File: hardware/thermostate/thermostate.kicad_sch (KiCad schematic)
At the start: 17 parts

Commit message: Finnish ESP32 SCH, NOT revision
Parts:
- added C1, C2: 0.1uF/50V(20%), symbol Device:C
- added D5: SK6812MINI, LED_SMD:LED_SK6812MINI_PLCC4_3.5x3.5mm_P1.75mm, symbol LED:SK6812MINI
- added IC1, IC2: L8050QLT1G, L8050QLT1G, symbol L8050QLT1G:L8050QLT1G
- added R1, R2: 10k(1%), symbol Device:R
- added R4, R5: 0(1%), symbol Device:R
- added SW1, SW2: SW_Push, symbol Switch:SW_Push
- gave numbers to parts that had none: 17
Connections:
- net +3V3: now also D5.4 (VDD)
- net CHIP_PU: now also C2.2, R4.1, SW2.2
- net GND: now also C1.1, C2.1, D5.2 (VSS), SW1.1, SW2.1
- net GPIO0: now reaches U1.27 (GPIO0/BOOT)
- net GPIO0: now also C1.2, R5.1, SW1.2
- net GPIO38: now reaches U1.31 (GPIO38/FSPIWP/SUBSPIWP)
- net GPIO38: now also D5.1 (DOUT)
- new net: IC1.1 (B), R1.2
- new net: IC1.3 (C), R4.2
- new net: IC2.3 (C), R5.2
- new net DTR: IC2.1 (B), IC2.2 (E), R1.1, R2.2
- new net RTS: IC1.2 (E), R2.1
- no-connect marks 1 -> 2
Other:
- moved on the sheet: C3, C4

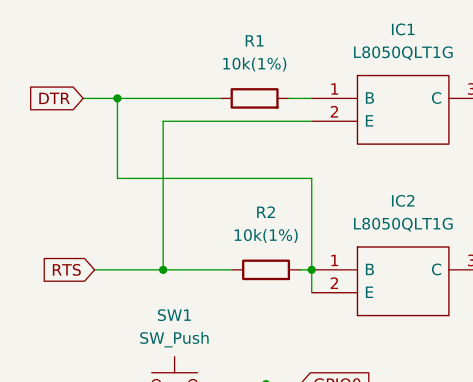
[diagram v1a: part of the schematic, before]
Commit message: Add LCSC row
Signed-off-by: Javier <javierfernandezvillasante@gmail.com>
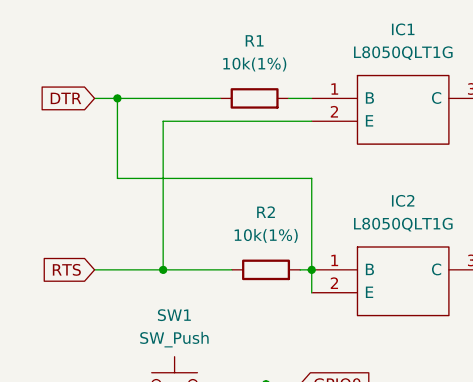
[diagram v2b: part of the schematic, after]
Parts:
- R1, R2: footprint (none) -> Resistor_SMD:R_0805_2012Metric; LCSC Part# (none) -> C269742
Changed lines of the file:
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@@
     (stroke (width 0) (type default) (color 0 0 0 0))
   )
-  (wire (pts (xy 22.86 34.29) (xy 19.05 34.29))
+  (wire (pts (xy 22.86 34.29) (xy 20.32 34.29))
     (stroke (width 0) (type default) (color 0 0 0 0))
   )
@@
     )
   )
-  (global_label "DTR" (shape input) (at 19.05 34.29 180) (fields_autoplaced)
+  (global_label "DTR" (shape input) (at 20.32 34.29 180) (fields_autoplaced)
     (effects (font (size 1.27 1.27)) (justify right))
-    (property "Intersheet References" "${INTERSHEET_REFS}" (id 0) (at 13.1293 34.2106 0)
+    (property "Intersheet References" "${INTERSHEET_REFS}" (id 0) (at 14.3993 34.2106 0)
       (effects (font (size 1.27 1.27)) (justify right) hide)
     )
@@
     (property "Reference" "R2" (id 0) (at 39.37 46.99 90))
     (property "Value" "10k(1%)" (id 1) (at 39.37 49.53 90))
-    (property "Footprint" "" (id 2) (at 39.37 55.118 90)
+    (property "Footprint" "Resistor_SMD:R_0805_2012Metric" (id 2) (at 39.37 55.118 90)
       (effects (font (size 1.27 1.27)) hide)
     )
     (property "Datasheet" "~" (id 3) (at 39.37 53.34 0)
+      (effects (font (size 1.27 1.27)) hide)
+    )
+    (property "LCSC Part#" "C269742" (id 4) (at 39.37 53.34 0)
       (effects (font (size 1.27 1.27)) hide)
     )
@@
     (property "Reference" "R1" (id 0) (at 38.1 27.94 90))
     (property "Value" "10k(1%)" (id 1) (at 38.1 30.48 90))
-    (property "Footprint" "" (id 2) (at 38.1 36.068 90)
+    (property "Footprint" "Resistor_SMD:R_0805_2012Metric" (id 2) (at 38.1 36.068 90)
       (effects (font (size 1.27 1.27)) hide)
     )
     (property "Datasheet" "~" (id 3) (at 38.1 34.29 0)
+      (effects (font (size 1.27 1.27)) hide)
+    )
+    (property "LCSC Part#" "C269742" (id 4) (at 38.1 34.29 0)
       (effects (font (size 1.27 1.27)) hide)
     )
@@
     )
     (path "/db62e411-33c3-4ab0-8164-8a94bc0d2a11"
-      (reference "R1") (unit 1) (value "10k(1%)") (footprint "")
+      (reference "R1") (unit 1) (value "10k(1%)") (footprint "Resistor_SMD:R_0805_2012Metric")
     )
     (path "/7cf1150b-1ddb-446b-8d01-6a50a54eec22"
-      (reference "R2") (unit 1) (value "10k(1%)") (footprint "")
+      (reference "R2") (unit 1) (value "10k(1%)") (footprint "Resistor_SMD:R_0805_2012Metric")
     )
     (path "/26f19b47-4227-4fff-aaee-0cd0c32318a2"

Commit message: Add LCSC reference some components
Signed-off-by: Javier <javierfernandezvillasante@gmail.com>
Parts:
- C1, C2: footprint (none) -> Capacitor_SMD:C_0805_2012Metric_Pad1.18x1.45mm_HandSolder; LCSC Part# (none) -> C138340
- C3, C5, C7: footprint (none) -> Capacitor_SMD:C_0805_2012Metric_Pad1.18x1.45mm_HandSolder; LCSC Part# (none) -> C669099
- C4: footprint (none) -> Capacitor_SMD:C_0805_2012Metric_Pad1.18x1.45mm_HandSolder; LCSC Part# (none) -> C2180294
- C6: footprint (none) -> Capacitor_SMD:C_0805_2012Metric_Pad1.18x1.45mm_HandSolder; LCSC Part# (none) -> C24123
- C8: footprint (none) -> Capacitor_SMD:C_0805_2012Metric_Pad1.18x1.45mm_HandSolder
- D1, D2, D4: footprint TVS_LESD5D5.0CT1G -> Diode_SMD:D_SOD-523; LCSC Part# (none) -> C5199850
- D3: footprint SOD3715X145N -> Diode_SMD:D_SOD-123; LCSC Part# (none) -> C82544
- D5: footprint LED_SMD:LED_SK6812MINI_PLCC4_3.5x3.5mm_P1.75mm -> LED_SMD:LED_Kingbright_AAA3528ESGCT; LCSC Part# (none) -> C2890038
- D6: footprint (none) -> LED_SMD:LED_0805_2012Metric_Pad1.15x1.40mm_HandSolder; LCSC Part# (none) -> C84256
- IC1, IC2: footprint L8050QLT1G -> Package_TO_SOT_SMD:SOT-23_Handsoldering; LCSC Part# (none) -> C49581
- P1: footprint (none) -> Connector_USB:USB_C_Receptacle_Amphenol_12401610E4-2A; LCSC Part# (none) -> C5299418
- R1, R2: footprint Resistor_SMD:R_0805_2012Metric -> Resistor_SMD:R_0805_2012Metric_Pad1.20x1.40mm_HandSolder
- R3, R7: footprint (none) -> Resistor_SMD:R_0805_2012Metric_Pad1.20x1.40mm_HandSolder; LCSC Part# (none) -> C27834
- R4, R5: footprint (none) -> Resistor_SMD:R_0805_2012Metric_Pad1.20x1.40mm_HandSolder; LCSC Part# (none) -> C17477
- R6: footprint (none) -> Resistor_SMD:R_0805_2012Metric_Pad1.20x1.40mm_HandSolder; LCSC Part# (none) -> C17414
- SW1, SW2: footprint (none) -> Button_Switch_SMD:SW_Push_1P1T_NO_CK_KMR2
- U2: footprint (none) -> Package_TO_SOT_SMD:SOT-23_Handsoldering

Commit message: Add first PCB prototype
Signed-off-by: Javier <javierfernandezvillasante@gmail.com>
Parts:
- removed C1, C2: 0.1uF/50V(20%), Capacitor_SMD:C_0805_2012Metric_Pad1.18x1.45mm_HandSolder, symbol Device:C
- removed C3, C5, C7: 10uF/25V(20%), Capacitor_SMD:C_0805_2012Metric_Pad1.18x1.45mm_HandSolder, symbol Device:C
- removed C4: 0.1uF/25V(20%), Capacitor_SMD:C_0805_2012Metric_Pad1.18x1.45mm_HandSolder, symbol Device:C
- removed C6: 1uF/16V(10%), Capacitor_SMD:C_0805_2012Metric_Pad1.18x1.45mm_HandSolder, symbol Device:C
- removed C8: 100uF/25V(20%), Capacitor_SMD:C_0805_2012Metric_Pad1.18x1.45mm_HandSolder, symbol Device:C
- removed D1, D2, D4: LESD5D5.0CT1G, Diode_SMD:D_SOD-523, symbol LESD5D5.0CT1G:LESD5D5.0CT1G
- removed D3: 1N5819HW-7-F, Diode_SMD:D_SOD-123, symbol 1N5819HW-7-F:1N5819HW-7-F
- removed D5: SK6812MINI, LED_SMD:LED_Kingbright_AAA3528ESGCT, symbol LED:SK6812MINI
- removed D6: RED LED, LED_SMD:LED_0805_2012Metric_Pad1.15x1.40mm_HandSolder, symbol Device:LED
- removed IC1, IC2: L8050QLT1G, Package_TO_SOT_SMD:SOT-23_Handsoldering, symbol L8050QLT1G:L8050QLT1G
- removed P1: USB_C_Plug_USB2.0, Connector_USB:USB_C_Receptacle_Amphenol_12401610E4-2A, symbol Connector:USB_C_Plug_USB2.0
- removed R1, R2: 10k(1%), Resistor_SMD:R_0805_2012Metric_Pad1.20x1.40mm_HandSolder, symbol Device:R
- removed R3, R7: 5.1k, Resistor_SMD:R_0805_2012Metric_Pad1.20x1.40mm_HandSolder, symbol Device:R
- removed R4, R5: 0(1%), Resistor_SMD:R_0805_2012Metric_Pad1.20x1.40mm_HandSolder, symbol Device:R
- removed R6: 10k (1%), Resistor_SMD:R_0805_2012Metric_Pad1.20x1.40mm_HandSolder, symbol Device:R
- removed SW1, SW2: SW_Push, Button_Switch_SMD:SW_Push_1P1T_NO_CK_KMR2, symbol Switch:SW_Push
- removed U1: ESP32-S3-WROOM-1, Espressif:ESP32-S3-WROOM-1, symbol Espressif:ESP32-S3-WROOM-1
- removed U2: LM1117-3.3, Package_TO_SOT_SMD:SOT-23_Handsoldering, symbol Regulator_Linear:LM1117-3.3
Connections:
- no-connect marks 2 -> 0
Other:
- added sheet ESP32_minimal (ESP32_minimal.kicad_sch)
- added sheet ExternalPush (ExternalPush.kicad_sch)
- note removed: "5V to 3V3"
- note removed: "USB"

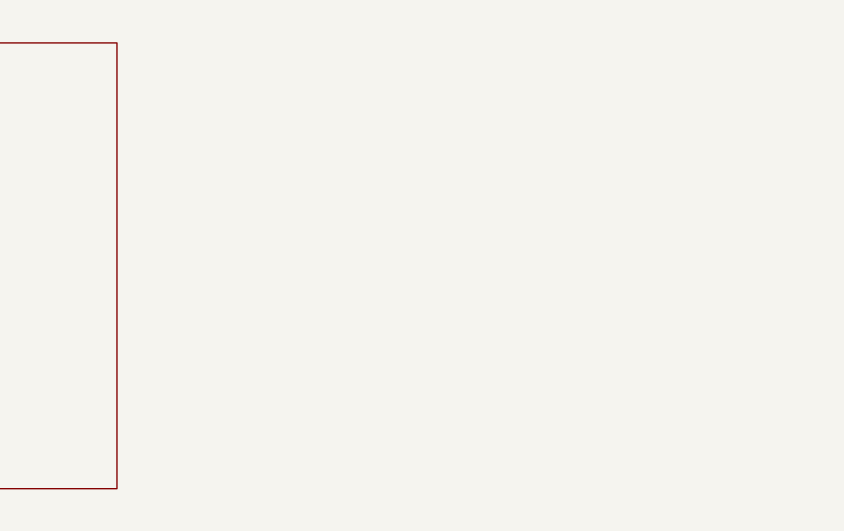
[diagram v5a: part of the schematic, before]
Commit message: Add Components PCB
Signed-off-by: Javier <javierfernandezvillasante@gmail.com>
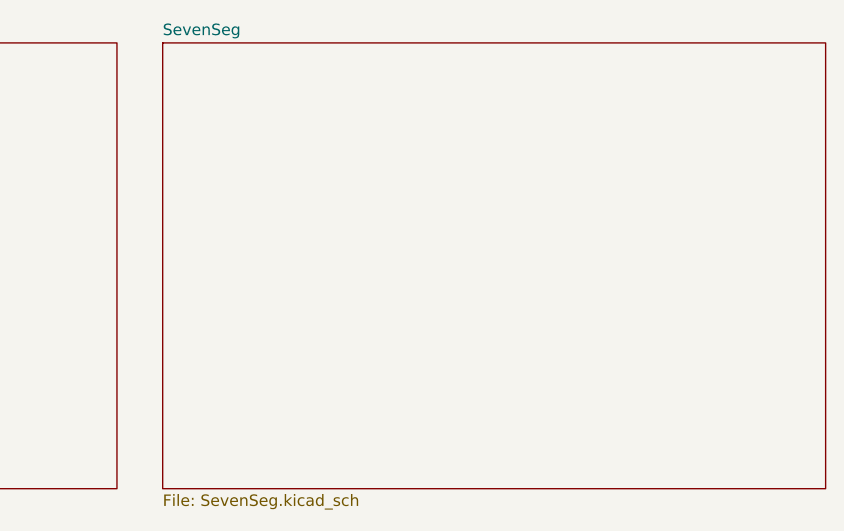
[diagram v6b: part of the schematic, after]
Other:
- added sheet SevenSeg (SevenSeg.kicad_sch)
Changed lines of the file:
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@@
 (kicad_sch (version 20211123) (generator eeschema)
   (paper "A4")
+  (sheet (at 193.04 25.4) (size 73.66 49.53) (fields_autoplaced)
+    (stroke (width 0.1524) (type solid) (color 0 0 0 0))
+    (fill (color 0 0 0 0.0000))
+    (property "Sheet name" "SevenSeg" (id 0) (at 193.04 24.6884 0)
+      (effects (font (size 1.27 1.27)) (justify left bottom))
+    )
+    (property "Sheet file" "SevenSeg.kicad_sch" (id 1) (at 193.04 75.5146 0)
+      (effects (font (size 1.27 1.27)) (justify left top))
+    )
+  )
   (sheet (at 114.3 25.4) (size 73.66 49.53) (fields_autoplaced)
     (stroke (width 0.1524) (type solid) (color 0 0 0 0))
@@
     (path "/dd42c31c-5aca-4c52-93b8-ef7d4a29cc26" (page "2"))
     (path "/9daf8fee-cd8e-47ee-84c9-ffcb9f8b22f1" (page "4"))
+    (path "/1f4f2a57-6ec8-4876-9c56-45d47cafb512" (page "5"))
   )
   (symbol_instances
@@
       (reference "#PWR0116") (unit 1) (value "+3V3") (footprint "")
     )
+    (path "/1f4f2a57-6ec8-4876-9c56-45d47cafb512/a457b8b5-c765-478b-a736-98499909655a"
+      (reference "#PWR0117") (unit 1) (value "+3V3") (footprint "")
+    )
+    (path "/1f4f2a57-6ec8-4876-9c56-45d47cafb512/6b3b12ec-18a9-4029-8fa2-4558e5746cf5"
+      (reference "#PWR0118") (unit 1) (value "+3V3") (footprint "")
+    )
+    (path "/1f4f2a57-6ec8-4876-9c56-45d47cafb512/d2cee3ce-4dde-4174-9a07-93a3c5bcdd19"
+      (reference "#PWR0119") (unit 1) (value "GND") (footprint "")
+    )
+    (path "/1f4f2a57-6ec8-4876-9c56-45d47cafb512/a6b49f93-c7ab-4a94-8885-388940b6fa3e"
+      (reference "#PWR0120") (unit 1) (value "+3V3") (footprint "")
+    )
     (path "/dd42c31c-5aca-4c52-93b8-ef7d4a29cc26/b93db3b6-c04f-47c4-80c4-9cb44da7a42e"
       (reference "C1") (unit 1) (value "0.1uF/50V(20%)") (footprint "Capacitor_SMD:C_0805_2012Metric_Pad1.18x1.45mm_HandSolder")
@@
       (reference "P1") (unit 1) (value "USB_C_Plug_USB2.0") (footprint "Connector_USB:USB_C_Receptacle_Amphenol_12401610E4-2A")
     )
+    (path "/1f4f2a57-6ec8-4876-9c56-45d47cafb512/a78b6c46-2a24-48bd-94a0-4db9275c74a3"
+      (reference "Q1") (unit 1) (value "BC847") (footprint "Package_TO_SOT_SMD:SOT-23")
+    )
+    (path "/1f4f2a57-6ec8-4876-9c56-45d47cafb512/257ecb1c-1871-45fe-8df0-d6099ae21d6d"
+      (reference "Q2") (unit 1) (value "BC847") (footprint "Package_TO_SOT_SMD:SOT-23")
+    )
     (path "/dd42c31c-5aca-4c52-93b8-ef7d4a29cc26/e5d96fc1-b01b-4da5-8fce-8b078dcadf3a"
       (reference "R1") (unit 1) (value "10k(1%)") (footprint "Resistor_SMD:R_0805_2012Metric_Pad1.20x1.40mm_HandSolder")
@@
       (reference "R8") (unit 1) (value "4K7(20%)") (footprint "Resistor_SMD:R_0805_2012Metric_Pad1.20x1.40mm_HandSolder")
     )
+    (path "/1f4f2a57-6ec8-4876-9c56-45d47cafb512/09e50774-b01d-4183-a359-4429fd7a9878"
+      (reference "R9") (unit 1) (value "10k (1%)") (footprint "Resistor_SMD:R_0805_2012Metric_Pad1.20x1.40mm_HandSolder")
+    )
+    (path "/1f4f2a57-6ec8-4876-9c56-45d47cafb512/d10a00ff-318a-4faf-a23d-5369ca1ec454"
+      (reference "R10") (unit 1) (value "10k (1%)") (footprint "Resistor_SMD:R_0805_2012Metric_Pad1.20x1.40mm_HandSolder")
+    )
     (path "/dd42c31c-5aca-4c52-93b8-ef7d4a29cc26/a58dbba4-79ec-4ab6-941d-b377269aee42"
       (reference "SW1") (unit 1) (value "SW_Push") (footprint "Button_Switch_SMD:SW_Push_1P1T_NO_CK_KMR2")
@@
       (reference "U3") (unit 1) (value "DS18B20") (footprint "Package_TO_SOT_THT:TO-92_Inline")
     )
-  )
+    (path "/1f4f2a57-6ec8-4876-9c56-45d47cafb512/2b96b59a-293c-4c5a-b2c8-12a31267ad41"
+      (reference "U5") (unit 1) (value "ELD-426SYGWA") (footprint "Display_7Segment:ELD_426XXXX")
+    )
+    (path "/1f4f2a57-6ec8-4876-9c56-45d47cafb512/49949091-4c8a-406d-8013-52e13817166d"
+      (reference "U6") (unit 1) (value "ULN2803A") (footprint "Package_DFN_QFN:QFN-20-1EP_4x4mm_P0.5mm_EP2.5x2.5mm")
+    )
+  )
